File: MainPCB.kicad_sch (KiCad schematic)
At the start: 34 parts, among them J1 RaspberryPi, J10 Conn_01x02, J2 Conn_01x02, J3 Screw_Terminal_01x02, J4 Conn_01x02, J5 Conn_01x06, J6 Conn_01x03_Pin, J7 Conn_01x10, J8 Conn_01x12, J9 Conn_01x04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

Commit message: Placed Components
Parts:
- removed D2: D_Photo, symbol Device:D_Photo
- removed J2: Conn_01x02, symbol Connector_Generic:Conn_01x02
- removed SW1, SW2, SW3, SW4, SW5, SW6, SW7: SW_SLIDE, symbol Switch:SW_Push
- added C1: 0.1uf, Capacitor_SMD:C_0603_1608Metric, symbol Device:C
- added J2: Conn_01x03, Connector_PinHeader_2.54mm:PinHeader_1x03_P2.54mm_Vertical, symbol Connector_Generic:Conn_01x03
- added SW1, SW2, SW3, SW4, SW5, SW6, SW7: SW_SPDT, SlideSW:SlideSwitch, symbol Switch:SW_SPDT
- added U6: TSOP25xx, PSR IR Sensors:TSSP4038, symbol Interface_Optical:TSOP25xx
- D1, J10: footprint (none) -> Connector_PinHeader_2.54mm:PinHeader_1x02_P2.54mm_Vertical
- J1, J9: footprint (none) -> Connector_PinHeader_2.54mm:PinHeader_1x04_P2.54mm_Vertical
- J3: footprint TerminalBlock_Phoenix:TerminalBlock_Phoenix_PT-1,5-2-5.0-H_1x02_P5.00mm_Horizontal -> SMDPads:Pads_1x02_XL
- J4: footprint PSR-Headers:1x02-Header -> Connector_PinHeader_2.54mm:PinHeader_1x02_P2.54mm_Vertical
- J6: footprint (none) -> Connector_PinHeader_2.54mm:PinHeader_1x03_P2.54mm_Vertical
- J7: footprint (none) -> Connector_PinHeader_2.54mm:PinHeader_2x05_P2.54mm_Vertical
- J8: footprint (none) -> Connector_PinHeader_2.54mm:PinHeader_2x06_P2.54mm_Vertical
- M1, M2, M3, M4: footprint (none) -> SMDPads:Pads_1x02_Large
- R1: value 470 -> 330; footprint (none) -> Resistor_THT:R_Axial_DIN0207_L6.3mm_D2.5mm_P10.16mm_Horizontal
- R2: footprint (none) -> Resistor_SMD:R_0805_2012Metric_Pad1.20x1.40mm_HandSolder
- U1: footprint (none) -> teensy:Teensy41
- U10: footprint CompassSensor:LIS3MDL -> Connector_PinHeader_2.54mm:PinHeader_1x04_P2.54mm_Vertical
- U11: value V_Regulator_-_5v -> V_Regulator5v; footprint TerminalBlock_Phoenix:TerminalBlock_Phoenix_PT-1,5-4-5.0-H_1x04_P5.00mm_Horizontal -> Connector_PinHeader_2.54mm:PinHeader_1x05_P2.54mm_Vertical
- U13: value V_Regulator_-_5v -> V_Regulator3.3v; footprint TerminalBlock_Phoenix:TerminalBlock_Phoenix_PT-1,5-4-5.0-H_1x04_P5.00mm_Horizontal -> Connector_PinHeader_2.54mm:PinHeader_1x05_P2.54mm_Vertical
- U2, U3, U4, U5: value ~ -> VNH Driver; footprint (none) -> MotorDriver:VNHDriver
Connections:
- net 12v is gone; now on net 12V: J6.2 (Pin_2)
- net 12V: now also U11.3 (IN+), U13.3 (IN+); no longer U11.1 (IN+), U13.1 (IN+)
- net 3.3V: now also U13.5 (OUT+), J2.2 (Pin_2), SW1.2 (B), SW2.2 (B), SW3.2 (B), SW4.2 (B), SW5.2 (B), SW6.2 (B), SW7.2 (B), U6.3 (GND); no longer U13.3 (OUT+)
- net 5V: now also U11.5 (OUT+); no longer R2.1, U11.3 (OUT+)
- net ESC: now also J2.3 (Pin_3)
- net GND: now also U1.34 (GND), C1.2, J2.1 (Pin_1), U6.2 (Vs); no longer U11.2 (IN-), U13.2 (IN-)
- net LightGate: now also C1.1
- net SLIDE1: now also SW1.1 (A)
- net SLIDE2: now also SW2.1 (A)
- net SLIDE3: now also SW3.1 (A)
- net SLIDE4: now also SW4.1 (A)
- net SLIDE5: now also SW7.1 (A)
- net SLIDE6: now also SW5.1 (A)
- net SLIDE7: now also SW6.1 (A)
- new net: R2.1, U6.1 (OUT)
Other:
- moved on the sheet: D1, U11, U13

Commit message: Routed Power Traces
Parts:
- J5: footprint Connectors:1X06 -> Connector_PinHeader_2.54mm:PinHeader_1x06_P2.54mm_Vertical
- SW1, SW2, SW3, SW4, SW5, SW6, SW7: footprint SlideSW:SlideSwitch -> SlideSW:SPDT_OS102011_CNK
- U12: footprint RockerSwitch:RockerSwitch-PSR -> RockerSwitch:DA102J12S215PQF
- U6: footprint PSR IR Sensors:TSSP4038 -> Connector_PinHeader_2.54mm:PinHeader_1x03_P2.54mm_Vertical
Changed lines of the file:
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@@
       (effects (font (size 1.27 1.27)) (justify left))
     )
-    (property "Footprint" "PSR IR Sensors:TSSP4038" (at 45.085 120.015 0)
+    (property "Footprint" "Connector_PinHeader_2.54mm:PinHeader_1x03_P2.54mm_Vertical" (at 45.085 120.015 0)
       (effects (font (size 1.27 1.27)) hide)
     )
@@
       (effects (font (size 1.27 1.27)))
     )
-    (property "Footprint" "SlideSW:SlideSwitch" (at 176.53 243.078 0)
+    (property "Footprint" "SlideSW:SPDT_OS102011_CNK" (at 176.53 243.078 0)
       (effects (font (size 1.27 1.27)) hide)
     )
@@
       (effects (font (size 1.27 1.27)))
     )
-    (property "Footprint" "SlideSW:SlideSwitch" (at 176.53 267.97 0)
+    (property "Footprint" "SlideSW:SPDT_OS102011_CNK" (at 176.53 267.97 0)
       (effects (font (size 1.27 1.27)) hide)
     )
@@
     (pin "3")
     (pin "4")
+    (pin "4")
     (pin "5")
-    (pin "4")
     (instances
       (project "MainPCB"
@@
       (effects (font (size 1.27 1.27)))
     )
-    (property "Footprint" "SlideSW:SlideSwitch" (at 176.022 208.28 0)
+    (property "Footprint" "SlideSW:SPDT_OS102011_CNK" (at 176.022 208.28 0)
       (effects (font (size 1.27 1.27)) hide)
     )
@@
       (effects (font (size 1.27 1.27)) (justify left))
     )
-    (property "Footprint" "RockerSwitch:RockerSwitch-PSR" (at 94.615 48.26 0)
+    (property "Footprint" "RockerSwitch:DA102J12S215PQF" (at 94.615 48.26 0)
       (effects (font (size 1.27 1.27)) hide)
     )
@@
       (effects (font (size 1.27 1.27)))
     )
-    (property "Footprint" "SlideSW:SlideSwitch" (at 175.768 218.948 0)
+    (property "Footprint" "SlideSW:SPDT_OS102011_CNK" (at 175.768 218.948 0)
       (effects (font (size 1.27 1.27)) hide)
     )
@@
       (effects (font (size 1.27 1.27)))
     )
-    (property "Footprint" "SlideSW:SlideSwitch" (at 177.292 255.27 0)
+    (property "Footprint" "SlideSW:SPDT_OS102011_CNK" (at 177.292 255.27 0)
       (effects (font (size 1.27 1.27)) hide)
     )
@@
       (effects (font (size 1.27 1.27)) (justify left))
     )
-    (property "Footprint" "Connectors:1X06" (at 36.195 238.76 0)
+    (property "Footprint" "Connector_PinHeader_2.54mm:PinHeader_1x06_P2.54mm_Vertical" (at 36.195 238.76 0)
       (effects (font (size 1.27 1.27)) hide)
     )
@@
     (pin "3")
     (pin "4")
+    (pin "4")
     (pin "5")
-    (pin "4")
     (instances
       (project "MainPCB"
@@
       (effects (font (size 1.27 1.27)))
     )
-    (property "Footprint" "SlideSW:SlideSwitch" (at 175.768 231.14 0)
+    (property "Footprint" "SlideSW:SPDT_OS102011_CNK" (at 175.768 231.14 0)
       (effects (font (size 1.27 1.27)) hide)
     )
@@
       (effects (font (size 1.27 1.27)))
     )
-    (property "Footprint" "SlideSW:SlideSwitch" (at 175.26 196.85 0)
-      (effects (font (size 1.27 1.27)) hide)
-    )
+    (property "Footprint" "SlideSW:SPDT_OS102011_CNK" (at 175.26 196.85 0)
+      (effects (font (size 1.27 1.27)) hide)
+    )

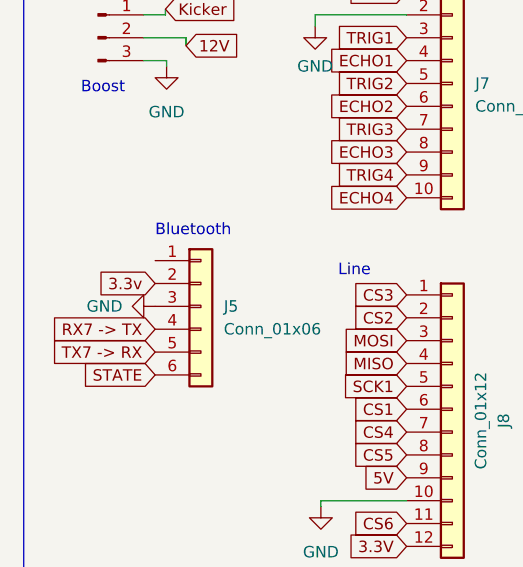
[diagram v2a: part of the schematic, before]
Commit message: Finished PCB
Finished Routing and added thermal zones
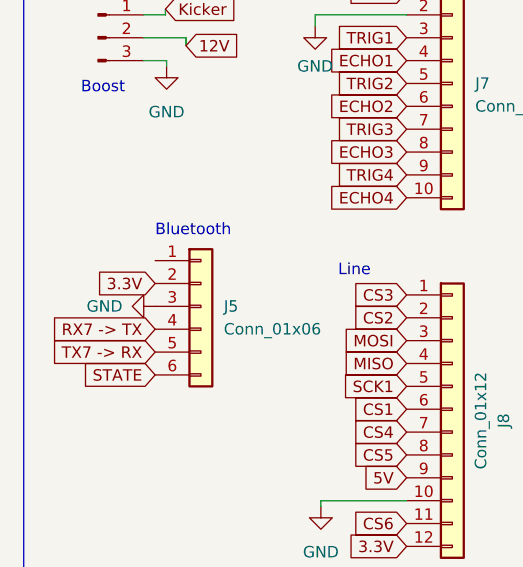
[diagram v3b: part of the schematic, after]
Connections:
- net 3.3v is gone; now on net 3.3V: J5.2 (Pin_2)
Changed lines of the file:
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@@
     )
   )
-  (global_label "3.3v" (shape input) (at 31.115 236.22 180) (fields_autoplaced)
+  (global_label "3.3V" (shape input) (at 31.115 236.22 180) (fields_autoplaced)
     (effects (font (size 1.27 1.27)) (justify right))
-    (property "Intersheetrefs" "${INTERSHEET_REFS}" (at 24.7105 236.2994 0)
+    (property "Intersheetrefs" "${INTERSHEET_REFS}" (at 24.0174 236.22 0)
       (effects (font (size 1.27 1.27)) (justify right) hide)
     )

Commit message: Changed Footprints
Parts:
- D1, J10, J4: footprint Connector_PinHeader_2.54mm:PinHeader_1x02_P2.54mm_Vertical -> Connector_JST:JST_EH_B2B-EH-A_1x02_P2.50mm_Vertical
- J1, J9, U10: footprint Connector_PinHeader_2.54mm:PinHeader_1x04_P2.54mm_Vertical -> Connector_JST:JST_EH_B4B-EH-A_1x04_P2.50mm_Vertical
- J2, J6, U6: footprint Connector_PinHeader_2.54mm:PinHeader_1x03_P2.54mm_Vertical -> Connector_JST:JST_EH_B3B-EH-A_1x03_P2.50mm_Vertical
- J7: footprint Connector_PinHeader_2.54mm:PinHeader_2x05_P2.54mm_Vertical -> Connector_IDC:IDC-Header_2x05_P2.54mm_Vertical
- J8: footprint Connector_PinHeader_2.54mm:PinHeader_2x06_P2.54mm_Vertical -> Connector_IDC:IDC-Header_2x06_P2.54mm_Vertical
- M1, M2, M3, M4: footprint SMDPads:Pads_1x02_Large -> Connector_JST:JST_EH_B2B-EH-A_1x02_P2.50mm_Vertical
- U12: footprint RockerSwitch:DA102J12S215PQF -> RockerSwitch:RG1-1A-DC-1-R-3
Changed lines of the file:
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@@
       (effects (font (size 1.27 1.27)) (justify left))
     )
-    (property "Footprint" "Connector_PinHeader_2.54mm:PinHeader_1x03_P2.54mm_Vertical" (at 45.085 120.015 0)
+    (property "Footprint" "Connector_JST:JST_EH_B3B-EH-A_1x03_P2.50mm_Vertical" (at 45.085 120.015 0)
       (effects (font (size 1.27 1.27)) hide)
     )
@@
       (effects (font (size 1.27 1.27)))
     )
-    (property "Footprint" "Connector_PinHeader_2.54mm:PinHeader_2x06_P2.54mm_Vertical" (at 64.135 250.19 0)
+    (property "Footprint" "Connector_IDC:IDC-Header_2x06_P2.54mm_Vertical" (at 64.135 250.19 0)
       (effects (font (size 1.27 1.27)) hide)
     )
@@
       (effects (font (size 1.27 1.27)) (justify left))
     )
-    (property "Footprint" "Connector_PinHeader_2.54mm:PinHeader_1x02_P2.54mm_Vertical" (at 241.935 233.045 0)
+    (property "Footprint" "Connector_JST:JST_EH_B2B-EH-A_1x02_P2.50mm_Vertical" (at 241.935 233.045 0)
       (effects (font (size 1.27 1.27)) hide)
     )
@@
       (effects (font (size 1.27 1.27)) (justify left))
     )
-    (property "Footprint" "RockerSwitch:DA102J12S215PQF" (at 94.615 48.26 0)
+    (property "Footprint" "RockerSwitch:RG1-1A-DC-1-R-3" (at 94.615 48.26 0)
       (effects (font (size 1.27 1.27)) hide)
     )
@@
       (effects (font (size 1.27 1.27)) (justify left))
     )
-    (property "Footprint" "Connector_PinHeader_2.54mm:PinHeader_1x02_P2.54mm_Vertical" (at 100.965 38.1 0)
+    (property "Footprint" "Connector_JST:JST_EH_B2B-EH-A_1x02_P2.50mm_Vertical" (at 100.965 38.1 0)
       (effects (font (size 1.27 1.27)) hide)
     )
@@
       (effects (font (size 1.27 1.27)) (justify left))
     )
-    (property "Footprint" "SMDPads:Pads_1x02_Large" (at 85.725 118.491 0)
+    (property "Footprint" "Connector_JST:JST_EH_B2B-EH-A_1x02_P2.50mm_Vertical" (at 85.725 118.491 0)
       (effects (font (size 1.27 1.27)) hide)
     )
@@
       (effects (font (size 1.27 1.27)) (justify left))
     )
-    (property "Footprint" "Connector_PinHeader_2.54mm:PinHeader_2x05_P2.54mm_Vertical" (at 64.135 213.995 0)
+    (property "Footprint" "Connector_IDC:IDC-Header_2x05_P2.54mm_Vertical" (at 64.135 213.995 0)
       (effects (font (size 1.27 1.27)) hide)
     )
@@
       (effects (font (size 1.27 1.27)) (justify left))
     )
-    (property "Footprint" "Connector_PinHeader_2.54mm:PinHeader_1x03_P2.54mm_Vertical" (at 241.3 219.202 0)
+    (property "Footprint" "Connector_JST:JST_EH_B3B-EH-A_1x03_P2.50mm_Vertical" (at 241.3 219.202 0)
       (effects (font (size 1.27 1.27)) hide)
     )
@@
       (effects (font (size 1.27 1.27)) (justify left))
     )
-    (property "Footprint" "SMDPads:Pads_1x02_Large" (at 85.725 96.901 0)
+    (property "Footprint" "Connector_JST:JST_EH_B2B-EH-A_1x02_P2.50mm_Vertical" (at 85.725 96.901 0)
       (effects (font (size 1.27 1.27)) hide)
     )
@@
       (effects (font (size 1.27 1.27)) (justify right))
     )
-    (property "Footprint" "Connector_PinHeader_2.54mm:PinHeader_1x02_P2.54mm_Vertical" (at 35.56 129.54 0)
+    (property "Footprint" "Connector_JST:JST_EH_B2B-EH-A_1x02_P2.50mm_Vertical" (at 35.56 129.54 0)
       (effects (font (size 1.27 1.27)) hide)
     )
@@
       (effects (font (size 1.27 1.27)) (justify left))
     )
-    (property "Footprint" "SMDPads:Pads_1x02_Large" (at 86.36 162.941 0)
+    (property "Footprint" "Connector_JST:JST_EH_B2B-EH-A_1x02_P2.50mm_Vertical" (at 86.36 162.941 0)
       (effects (font (size 1.27 1.27)) hide)
     )
@@
       (effects (font (size 1.27 1.27)) (justify left))
     )
-    (property "Footprint" "SMDPads:Pads_1x02_Large" (at 86.36 141.351 0)
+    (property "Footprint" "Connector_JST:JST_EH_B2B-EH-A_1x02_P2.50mm_Vertical" (at 86.36 141.351 0)
       (effects (font (size 1.27 1.27)) hide)
     )
@@
       (effects (font (size 1.27 1.27)))
     )
-    (property "Footprint" "Connector_PinHeader_2.54mm:PinHeader_1x03_P2.54mm_Vertical" (at 24.765 208.915 0)
+    (property "Footprint" "Connector_JST:JST_EH_B3B-EH-A_1x03_P2.50mm_Vertical" (at 24.765 208.915 0)
       (effects (font (size 1.27 1.27)) hide)
     )
@@
       (effects (font (size 1.27 1.27)))
     )
-    (property "Footprint" "Connector_PinHeader_2.54mm:PinHeader_1x04_P2.54mm_Vertical" (at 86.995 264.16 0)
+    (property "Footprint" "Connector_JST:JST_EH_B4B-EH-A_1x04_P2.50mm_Vertical" (at 86.995 264.16 0)
       (effects (font (size 1.27 1.27)) hide)
     )
@@
       (effects (font (size 1.27 1.27)) (justify left))
     )
-    (property "Footprint" "Connector_PinHeader_2.54mm:PinHeader_1x04_P2.54mm_Vertical" (at 99.695 205.74 0)
+    (property "Footprint" "Connector_JST:JST_EH_B4B-EH-A_1x04_P2.50mm_Vertical" (at 99.695 205.74 0)
       (effects (font (size 1.27 1.27)) hide)
     )
@@
       (effects (font (size 1.27 1.27)))
     )
-    (property "Footprint" "Connector_PinHeader_2.54mm:PinHeader_1x04_P2.54mm_Vertical" (at 85.09 238.76 0)
-      (effects (font (size 1.27 1.27)) hide)
-    )
+    (property "Footprint" "Connector_JST:JST_EH_B4B-EH-A_1x04_P2.50mm_Vertical" (at 85.09 238.76 0)
+      (effects (font (size 1.27 1.27)) hide)
+    )

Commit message: done
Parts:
- removed C1: 0.1uf, Capacitor_SMD:C_0603_1608Metric, symbol Device:C
- removed R2: 100k, Resistor_SMD:R_0805_2012Metric_Pad1.20x1.40mm_HandSolder, symbol Device:R
- added H1, H2, H3, H4: MountingHole, MountingHole:MountingHole_3.2mm_M3, symbol Mechanical:MountingHole
- added H5, H6, H7, H8: MountingHole, MountingHole:MountingHole_2.7mm_M2.5, symbol Mechanical:MountingHole
- D1, J10, J4, M1, M2, M3, M4: footprint Connector_JST:JST_EH_B2B-EH-A_1x02_P2.50mm_Vertical -> Connector_JST:JST_XH_B2B-XH-AM_1x02_P2.50mm_Vertical
- J1, J9: footprint Connector_JST:JST_EH_B4B-EH-A_1x04_P2.50mm_Vertical -> Connector_JST:JST_XH_B4B-XH-AM_1x04_P2.50mm_Vertical
- J2, J6, U6: footprint Connector_JST:JST_EH_B3B-EH-A_1x03_P2.50mm_Vertical -> Connector_JST:JST_XH_B3B-XH-AM_1x03_P2.50mm_Vertical
- U10: footprint Connector_JST:JST_EH_B4B-EH-A_1x04_P2.50mm_Vertical -> Connector_PinHeader_2.54mm:PinHeader_1x04_P2.54mm_Vertical
- U12: footprint RockerSwitch:RG1-1A-DC-1-R-3 -> RockerSwitch:RF1-1A-DC-2-B-2
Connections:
- net LightGate: now also U6.1 (OUT)
